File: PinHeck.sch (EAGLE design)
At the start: 328 parts, among them IC1 FT232RQ-REEL, IC2 PIC32MX795F512L-80I/PT, IC3 CD74HCT244E, IC4 CD74HCT244E, IC5 ULN2803A, J1 500075-1517, J11 No Load, J2 500075-1517, J3 N/A, J6 161-3507-E, P1 TC33X-2-103E, SW1 101-0134-EV, SW2 101-0134-EV, U1 P8X32A-Q44, U10 74HCT2G04GV,125, U11 74HC165D,652, U12 74HC165D,652, U14 MC74HC08ADG, U15 MC74HC08ADG, U16 MC74HC08ADG, U17 MC74HC08ADG, U18 MC74HC08ADG, U19 MC74HC08ADG, U2 FT230XS-R, U20 TIP107, U21 TIP107, U22 TIP107, U23 TIP107, U24 TIP107, U25 TIP107, U26 TIP107, U27 TIP107, U28 TIP102, U29 TIP102, U3 74HC595D-Q100, U30 TIP102, U31 TIP102, U32 TIP102, U33 TIP102, U34 TIP102, U35 TIP102, U36 WS2801, U37 TIP102, U38 WS2801, U39 LM2937IMP-3.3/NOPB, U4 CAT24M01XI-T2, U40 TIP102, U41 TIP102, U42 TIP102, U43 TIP102, U44 TIP102, U45 TIP102, U46 TIP102, U47 TIP102, U48 TIP102, U49 TIP102, U5 74HC595D-Q100, U50 TIP102, U51 TIP102, U52 CD74HC123M96, U6 TIP102, U7 TIP102, U8 TIP102, U9 TIP102, X1 FQ7050B-8.000, X2 ECS-65-20-4X

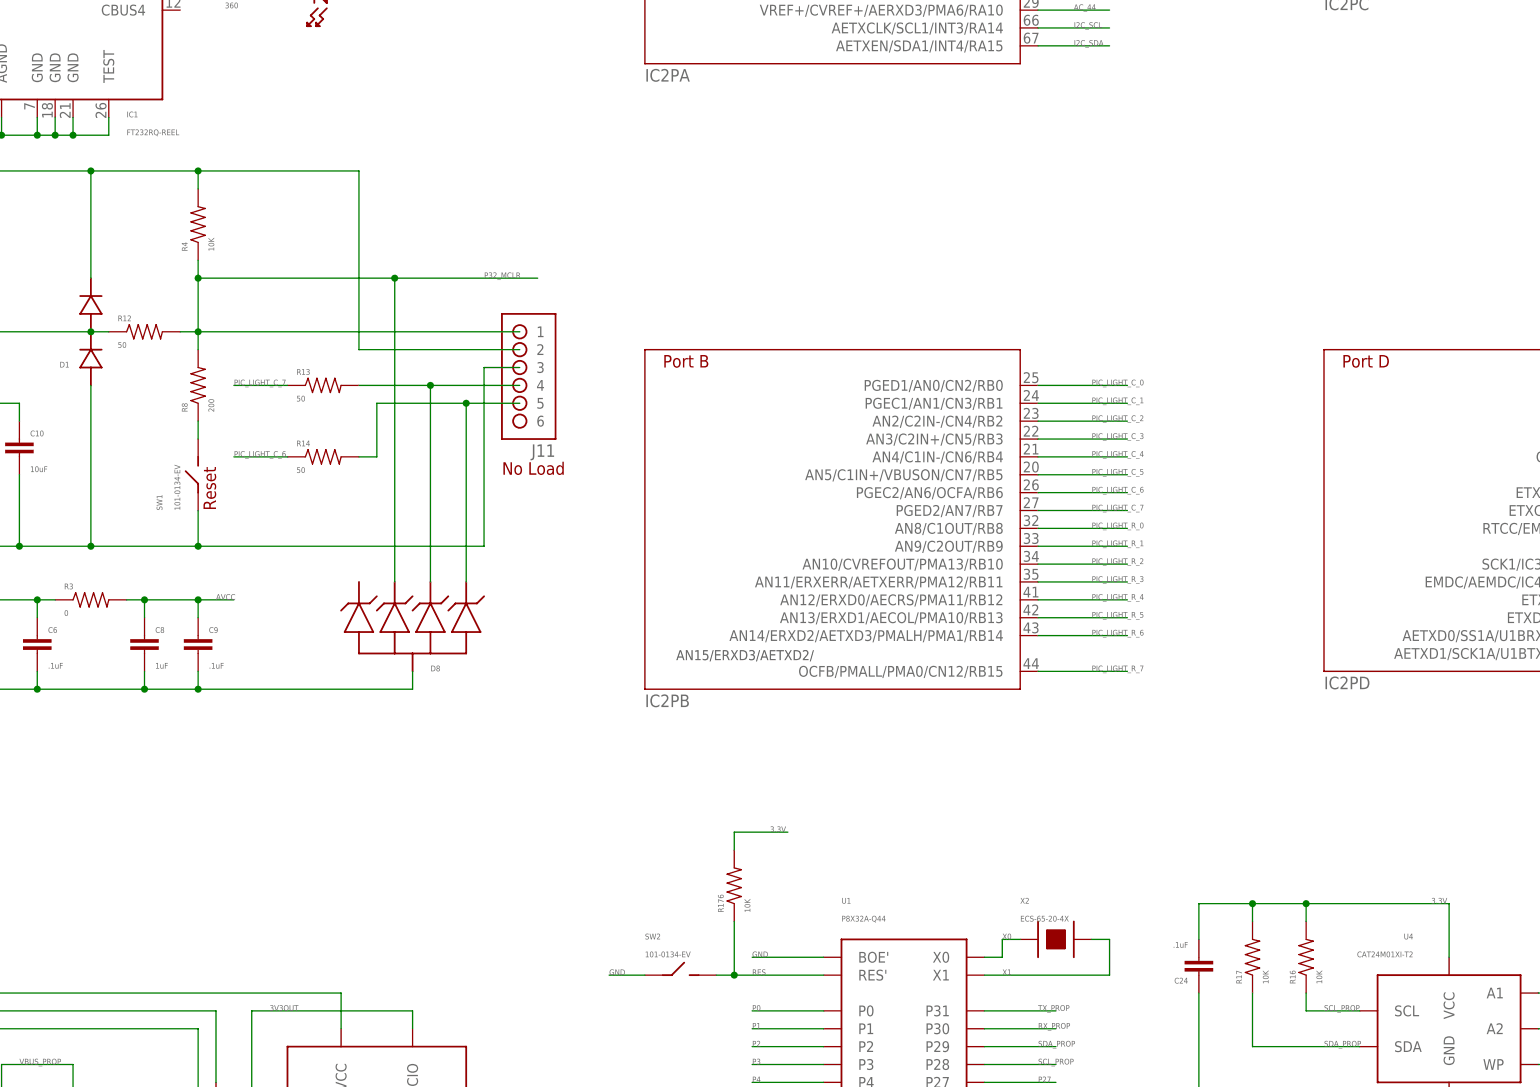
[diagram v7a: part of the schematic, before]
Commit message: Rev 5 push. Fixed Bom issues and pinout for 556.
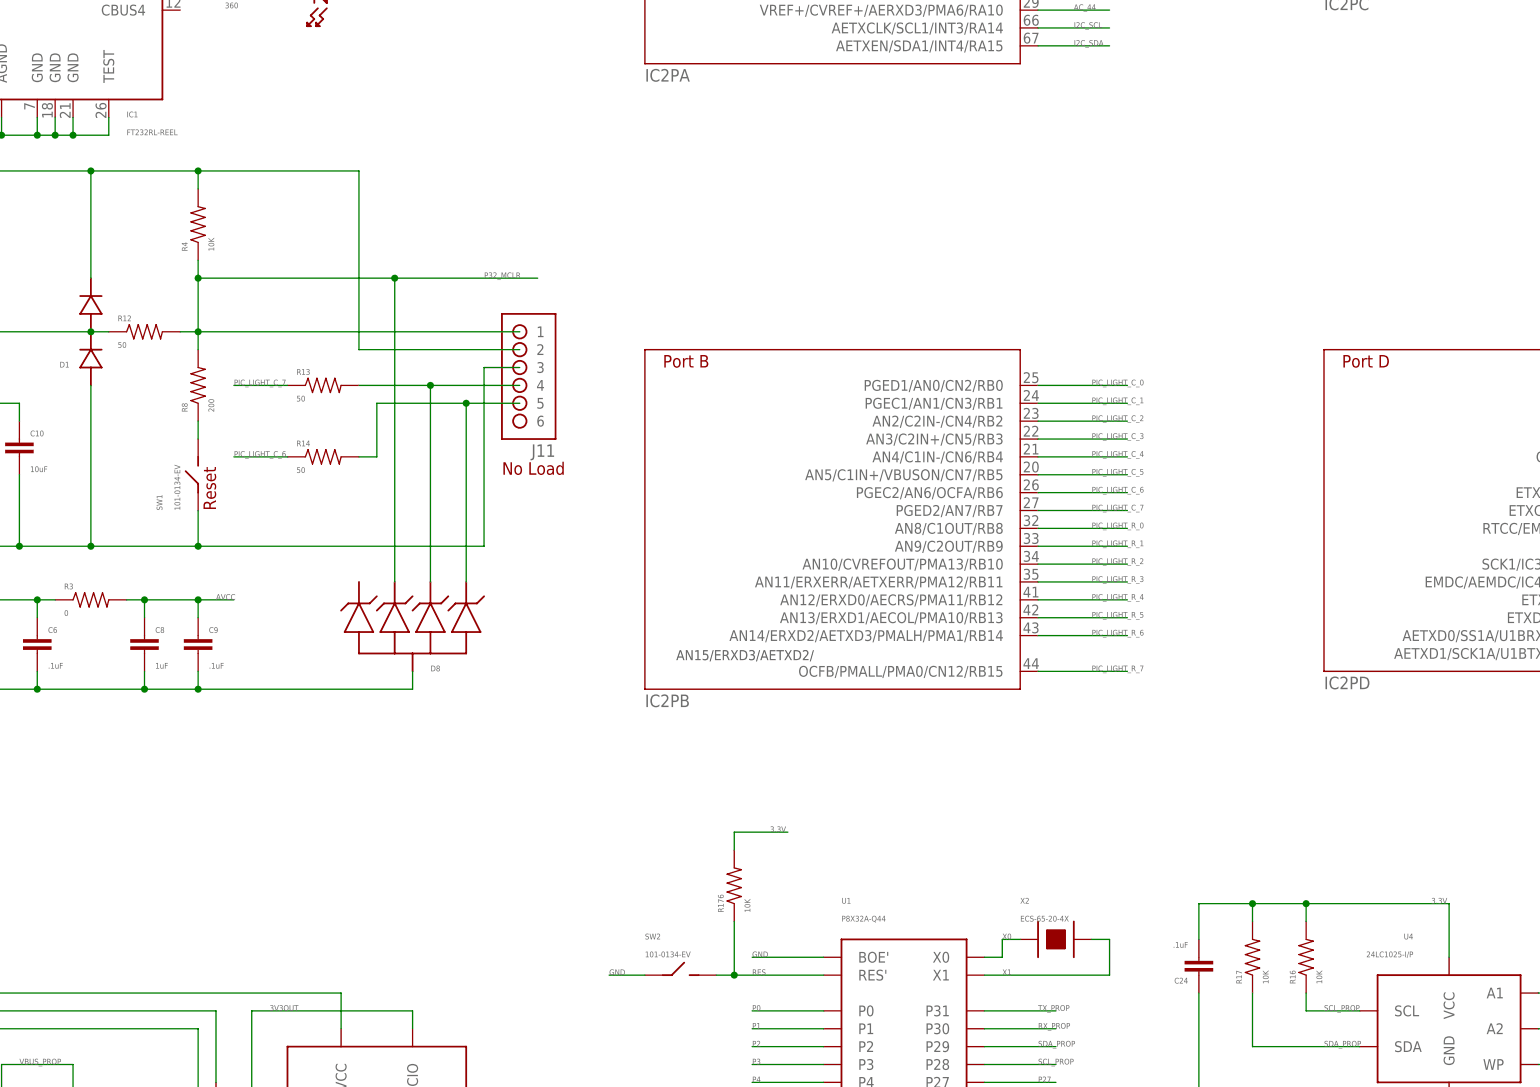
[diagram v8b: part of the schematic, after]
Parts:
- IC1: value FT232RQ-REEL -> FT232RL-REEL
- U4: value CAT24M01XI-T2 -> 24LC1025-I/P
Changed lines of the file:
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@@
 <?xml version="1.0" encoding="utf-8"?>
 <!DOCTYPE eagle SYSTEM "eagle.dtd">
-<eagle version="6.5.0">
+<eagle version="6.3">
 <drawing>
 <settings>
@@
 <grid distance="0.1" unitdist="inch" unit="inch" style="lines" multiple="1" display="no" altdistance="0.01" altunitdist="inch" altunit="inch"/>
 <layers>
-<layer number="1" name="Top" color="4" fill="1" visible="no" active="no"/>
-<layer number="2" name="Route2" color="1" fill="3" visible="no" active="no"/>
-<layer number="3" name="Route3" color="4" fill="3" visible="no" active="no"/>
-<layer number="4" name="Route4" color="1" fill="4" visible="no" active="no"/>
-<layer number="5" name="Route5" color="4" fill="4" visible="no" active="no"/>
-<layer number="6" name="Route6" color="1" fill="8" visible="no" active="no"/>
-<layer number="7" name="Route7" color="4" fill="8" visible="no" active="no"/>
-<layer number="8" name="Route8" color="1" fill="2" visible="no" active="no"/>
-<layer number="9" name="Route9" color="4" fill="2" visible="no" active="no"/>
-<layer number="10" name="Route10" color="1" fill="7" visible="no" active="no"/>
-<layer number="11" name="Route11" color="4" fill="7" visible="no" active="no"/>
-<layer number="12" name="Route12" color="1" fill="5" visible="no" active="no"/>
-<layer number="13" name="Route13" color="4" fill="5" visible="no" active="no"/>
-<layer number="14" name="Route14" color="1" fill="6" visible="no" active="no"/>
-<layer number="15" name="Route15" color="4" fill="6" visible="no" active="no"/>
-<layer number="16" name="Bottom" color="1" fill="1" visible="no" active="no"/>
-<layer number="17" name="Pads" color="2" fill="1" visible="no" active="no"/>
-<layer number="18" name="Vias" color="2" fill="1" visible="no" active="no"/>
-<layer number="19" name="Unrouted" color="6" fill="1" visible="no" active="no"/>
-<layer number="20" name="Dimension" color="15" fill="1" visible="no" active="no"/>
-<layer number="21" name="tPlace" color="7" fill="1" visible="no" active="no"/>
-<layer number="22" name="bPlace" color="7" fill="1" visible="no" active="no"/>
-<layer number="23" name="tOrigins" color="15" fill="1" visible="no" active="no"/>
-<layer number="24" name="bOrigins" color="15" fill="1" visible="no" active="no"/>
-<layer number="25" name="tNames" color="7" fill="1" visible="no" active="no"/>
-<layer number="26" name="bNames" color="7" fill="1" visible="no" active="no"/>
-<layer number="27" name="tValues" color="7" fill="1" visible="no" active="no"/>
-<layer number="28" name="bValues" color="7" fill="1" visible="no" active="no"/>
+<layer number="1" name="Top" color="4" fill="1" visible="yes" active="no"/>
+<layer number="2" name="Route2" color="1" fill="3" visible="yes" active="no"/>
+<layer number="3" name="Route3" color="4" fill="3" visible="yes" active="no"/>
+<layer number="4" name="Route4" color="1" fill="4" visible="yes" active="no"/>
+<layer number="5" name="Route5" color="4" fill="4" visible="yes" active="no"/>
+<layer number="6" name="Route6" color="1" fill="8" visible="yes" active="no"/>
+<layer number="7" name="Route7" color="4" fill="8" visible="yes" active="no"/>
+<layer number="8" name="Route8" color="1" fill="2" visible="yes" active="no"/>
+<layer number="9" name="Route9" color="4" fill="2" visible="yes" active="no"/>
+<layer number="10" name="Route10" color="1" fill="7" visible="yes" active="no"/>
+<layer number="11" name="Route11" color="4" fill="7" visible="yes" active="no"/>
+<layer number="12" name="Route12" color="1" fill="5" visible="yes" active="no"/>
+<layer number="13" name="Route13" color="4" fill="5" visible="yes" active="no"/>
+<layer number="14" name="Route14" color="1" fill="6" visible="yes" active="no"/>
+<layer number="15" name="Route15" color="4" fill="6" visible="yes" active="no"/>
+<layer number="16" name="Bottom" color="1" fill="1" visible="yes" active="no"/>
+<layer number="17" name="Pads" color="2" fill="1" visible="yes" active="no"/>
+<layer number="18" name="Vias" color="2" fill="1" visible="yes" active="no"/>
+<layer number="19" name="Unrouted" color="6" fill="1" visible="yes" active="no"/>
+<layer number="20" name="Dimension" color="15" fill="1" visible="yes" active="no"/>
+<layer number="21" name="tPlace" color="7" fill="1" visible="yes" active="no"/>
+<layer number="22" name="bPlace" color="7" fill="1" visible="yes" active="no"/>
+<layer number="23" name="tOrigins" color="15" fill="1" visible="yes" active="no"/>
+<layer number="24" name="bOrigins" color="15" fill="1" visible="yes" active="no"/>
+<layer number="25" name="tNames" color="7" fill="1" visible="yes" active="no"/>
+<layer number="26" name="bNames" color="7" fill="1" visible="yes" active="no"/>
+<layer number="27" name="tValues" color="7" fill="1" visible="yes" active="no"/>
+<layer number="28" name="bValues" color="7" fill="1" visible="yes" active="no"/>
 <layer number="29" name="tStop" color="7" fill="3" visible="no" active="no"/>
 <layer number="30" name="bStop" color="7" fill="6" visible="no" active="no"/>
@@
 <layer number="35" name="tGlue" color="7" fill="4" visible="no" active="no"/>
 <layer number="36" name="bGlue" color="7" fill="5" visible="no" active="no"/>
-<layer number="37" name="tTest" color="7" fill="1" visible="no" active="no"/>
-<layer number="38" name="bTest" color="7" fill="1" visible="no" active="no"/>
+<layer number="37" name="tTest" color="7" fill="1" visible="yes" active="no"/>
+<layer number="38" name="bTest" color="7" fill="1" visible="yes" active="no"/>
 <layer number="39" name="tKeepout" color="4" fill="11" visible="no" active="no"/>
 <layer number="40" name="bKeepout" color="1" fill="11" visible="no" active="no"/>
@@
 <layer number="44" name="Drills" color="7" fill="1" visible="no" active="no"/>
 <layer number="45" name="Holes" color="7" fill="1" visible="no" active="no"/>
-<layer number="46" name="Milling" color="3" fill="1" visible="no" active="no"/>
-<layer number="47" name="Measures" color="7" fill="1" visible="no" active="no"/>
-<layer number="48" name="Document" color="7" fill="1" visible="no" active="no"/>
-<layer number="49" name="Reference" color="7" fill="1" visible="no" active="no"/>
-<layer number="50" name="dxf" color="7" fill="1" visible="no" active="no"/>
-<layer number="51" name="tDocu" color="7" fill="1" visible="no" active="no"/>
-<layer number="52" name="bDocu" color="7" fill="1" visible="no" active="no"/>
-<layer number="53" name="tGND_GNDA" color="7" fill="9" visible="no" active="no"/>
-<layer number="54" name="bGND_GNDA" color="1" fill="9" visible="no" active="no"/>
-<layer number="56" name="wert" color="7" fill="1" visible="no" active="no"/>
+<layer number="46" name="Milling" color="3" fill="1" visible="yes" active="no"/>
+<layer number="47" name="Measures" color="7" fill="1" visible="yes" active="no"/>
+<layer number="48" name="Document" color="7" fill="1" visible="yes" active="no"/>
+<layer number="49" name="Reference" color="7" fill="1" visible="yes" active="no"/>
+<layer number="50" name="dxf" color="7" fill="1" visible="yes" active="no"/>
+<layer number="51" name="tDocu" color="7" fill="1" visible="yes" active="no"/>
+<layer number="52" name="bDocu" color="7" fill="1" visible="yes" active="no"/>
+<layer number="53" name="tGND_GNDA" color="7" fill="9" visible="yes" active="no"/>
+<layer number="54" name="bGND_GNDA" color="1" fill="9" visible="yes" active="no"/>
+<layer number="56" name="wert" color="7" fill="1" visible="yes" active="no"/>
 <layer number="91" name="Nets" color="2" fill="1" visible="yes" active="yes"/>
 <layer number="92" name="Busses" color="1" fill="1" visible="yes" active="yes"/>
@@
 </classes>
 <parts>
-<part name="IC1" library="IC" deviceset="FT232R" device="L" value="FT232RQ-REEL"/>
+<part name="IC1" library="IC" deviceset="FT232R" device="L" value="FT232RL-REEL"/>
 <part name="IC2" library="Microchip" deviceset="PIC32MX7X5F*L" device="-PT" value="PIC32MX795F512L-80I/PT"/>
 <part name="D1" library="Discrete" deviceset="BAV99W" device="" value="BAV99W,115"/>
@@
 <part name="SW2" library="PP_Electromechanical" deviceset="SPST" device="101-0134-EV" value="101-0134-EV"/>
 <part name="R176" library="PP_Passives" deviceset="RESISTOR" device="0805" value="10K"/>
-<part name="U4" library="PP_DigitalIC" deviceset="CAT24M01XI-T2" device="DIP-8" value="CAT24M01XI-T2"/>
+<part name="U4" library="PP_DigitalIC" deviceset="CAT24M01XI-T2" device="DIP-8" value="24LC1025-I/P"/>
 <part name="R16" library="PP_Passives" deviceset="RESISTOR" device="0805" value="10K"/>
 <part name="R17" library="PP_Passives" deviceset="RESISTOR" device="0805" value="10K"/>
